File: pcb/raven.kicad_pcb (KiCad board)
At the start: 4 copper layers, 63.2 x 54.2 mm, 144 parts, among them J1 Conn_02x20_Odd_Even, J11 Screw_Terminal_01x10, J14 Conn_01x04_Pin, J15 Conn_01x04_Pin, J16 Conn_01x04_Pin, J17 Conn_01x04_Pin, J18 Conn_01x04_Pin, J2 Conn_01x04_MountingPin, J21 Conn_01x03_Pin, J22 Conn_01x03_Pin, J23 Conn_01x03_Pin, J24 Conn_01x03_Pin, J25 Conn_01x03_Pin, J3 Conn_01x02_Pin, J4 Conn_01x02_Pin, J5 Conn_01x04_MountingPin, J6 Conn_01x02_Pin, J7 Conn_01x02_Pin, J8 Conn_01x02_Pin, J9 Conn_01x02_Pin, U1 DRV8874PWPR, U2 ICM-42688-P, U3 QMC5883L, U30 DRV8874PWPR, U4 DRV8874PWPR, U5 DRV8874PWPR, U6 DRV8874PWPR, U7 STM32G431CBUx, U8 74HC595, Y1 16MHz

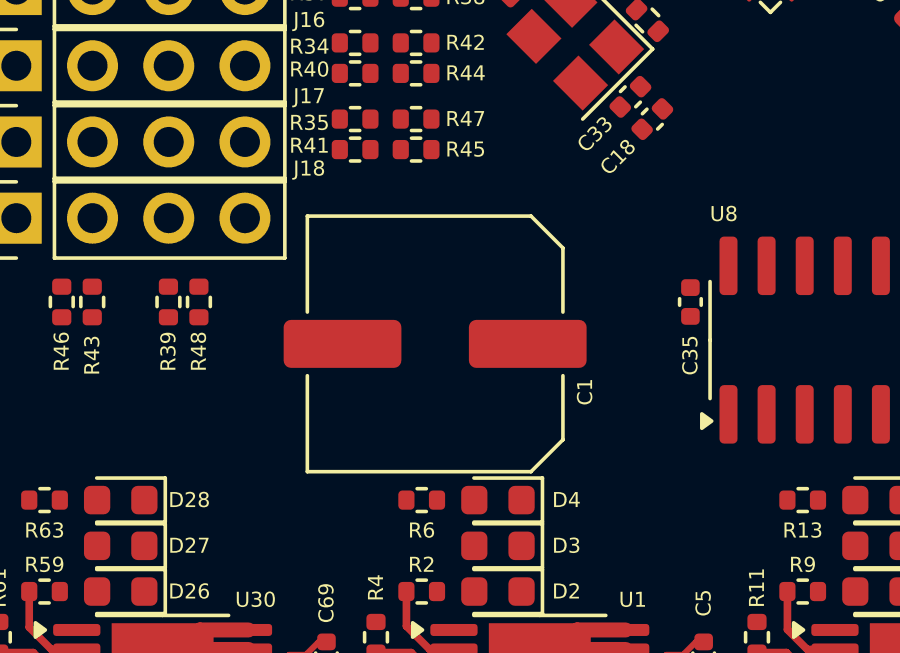
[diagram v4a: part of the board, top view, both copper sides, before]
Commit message: Start on regulator
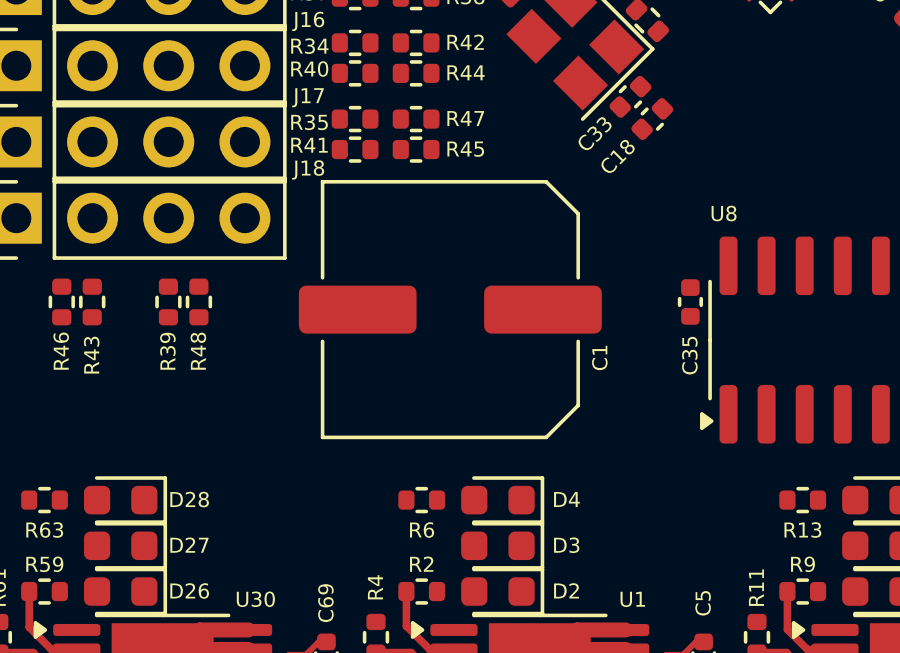
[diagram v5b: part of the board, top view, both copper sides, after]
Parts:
- moved C1 1.25 mm to (113.2, 75.4)

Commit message: Save progress
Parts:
- added C23: 100n, Capacitor_SMD:C_0603_1608Metric, F.Cu at (144.0, 80.4)
- added C39: 100n, Capacitor_SMD:C_0402_1005Metric, F.Cu at (143.2, 71.6)
- added C40: 47u, Capacitor_SMD:C_1206_3216Metric, F.Cu at (142.6, 69.8)
- added C41: 47u, Capacitor_SMD:C_1206_3216Metric, F.Cu at (142.6, 67.4)
- added C42: 47u, Capacitor_SMD:C_1206_3216Metric, F.Cu at (142.6, 65.0)
- added C43: 47u, Capacitor_SMD:C_1206_3216Metric, F.Cu at (142.6, 62.6)
- added C44: 220n, Capacitor_SMD:C_0603_1608Metric, F.Cu at (148.3, 83.4)
- added C45: 2u2, Capacitor_SMD:C_0805_2012Metric, F.Cu at (144.0, 74.0)
- added C46: 1u, Capacitor_SMD:C_0402_1005Metric, F.Cu at (144.4, 78.4)
- added C47: 1u, Capacitor_SMD:C_0402_1005Metric, F.Cu at (143.4, 78.4)
- added C48: 1u, Capacitor_SMD:C_0402_1005Metric, F.Cu at (150.4, 77.0)
- added C49: 1u, Capacitor_SMD:C_0402_1005Metric, F.Cu at (151.4, 77.0)
- added C50: 22u, Capacitor_SMD:C_0805_2012Metric, F.Cu at (153.0, 76.8)
- added C51: 22u, Capacitor_SMD:C_0805_2012Metric, F.Cu at (155.0, 76.8)
- added C52: 22u, Capacitor_SMD:C_0805_2012Metric, F.Cu at (157.0, 76.8)
- added C53: 22u, Capacitor_SMD:C_0805_2012Metric, F.Cu at (159.0, 76.8)
- added C54: 22u, Capacitor_SMD:C_0805_2012Metric, F.Cu at (157.0, 79.5)
- added C57: 22u, Capacitor_SMD:C_0805_2012Metric, F.Cu at (119.0, 82.6)
- added C58: 22u, Capacitor_SMD:C_0805_2012Metric, F.Cu at (131.6, 82.6)
- added C59: 22u, Capacitor_SMD:C_0805_2012Metric, F.Cu at (131.6, 84.6)
- added C60: 22u, Capacitor_SMD:C_0805_2012Metric, F.Cu at (144.0, 82.6)
- added C61: 22u, Capacitor_SMD:C_0805_2012Metric, F.Cu at (144.0, 84.6)
- added C62: 22u, Capacitor_SMD:C_0805_2012Metric, F.Cu at (157.0, 82.5)
- added C63: 22u, Capacitor_SMD:C_0805_2012Metric, F.Cu at (157.0, 84.5)
- added C64: 22u, Capacitor_SMD:C_0805_2012Metric, F.Cu at (106.4, 82.6)
- added C65: 22u, Capacitor_SMD:C_0805_2012Metric, F.Cu at (106.4, 84.6)
- added D14: GLED, LED_SMD:LED_0603_1608Metric, F.Cu at (136.6, 70.2)
- added L1: 330nH, Inductor_SMD:L_Changjiang_FXL0630, F.Cu at (138.6, 75.4)
- added R28: R, Resistor_SMD:R_0402_1005Metric, F.Cu at (146.4, 81.7)
- added R49: R, Resistor_SMD:R_0402_1005Metric, F.Cu at (147.4, 81.7)
- added R50: 1k, Resistor_SMD:R_0402_1005Metric, F.Cu at (139.1, 70.4)
- added R51: R, Resistor_SMD:R_0402_1005Metric, F.Cu at (158.3, 81.0)
- added R52: R, Resistor_SMD:R_0402_1005Metric, F.Cu at (156.2, 81.0)
- added R53: R, Resistor_SMD:R_0402_1005Metric, F.Cu at (149.8, 81.7)
- added R54: R, Resistor_SMD:R_0402_1005Metric, F.Cu at (148.8, 81.7)
- added R55: 10k, Resistor_SMD:R_0402_1005Metric, F.Cu at (102.1, 79.7)
- added SW1: SW_Push, Footprints:TS-1088, F.Cu at (99.4, 77.2)
- added SW2: SW_Push, Footprints:TS-1088, F.Cu at (104.8, 77.2)
- added U9: TPS548B28RWWR, Footprints:TPS548B28RWWR, F.Cu at (147.4, 77.4)
- C13: value 100u -> 22u; footprint Capacitor_SMD:C_Elec_8x6.2 -> Capacitor_SMD:C_0805_2012Metric
- moved J9 23.0 mm to (138.0, 67.2), turned to -90 degrees
- moved C13 23.0 mm to (119.0, 84.6), turned to 180 degrees
- moved J4 22.4 mm to (138.0, 57.0), turned to -90 degrees
- moved J8 22.0 mm to (138.0, 64.6), turned to -90 degrees
- moved J6 21.7 mm to (138.0, 59.5), turned to -90 degrees
- moved J7 21.5 mm to (138.0, 62.1), turned to -90 degrees
- moved R24 8.70 mm to (128.2, 70.2), turned to 90 degrees
- moved R25 8.35 mm to (131.2, 70.2)
- moved C28 7.14 mm to (133.6, 72.4), turned to 180 degrees
- moved J22 5.94 mm to (144.6, 54.5)
- moved J21 5.94 mm to (142.0, 54.5)
- moved J23 5.94 mm to (147.1, 54.5)
- moved J24 5.94 mm to (149.7, 54.5)
- moved J25 5.94 mm to (152.2, 54.5)
- moved R39 3.19 mm to (107.0, 75.2)
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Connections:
- net /BOOT renamed /BT0

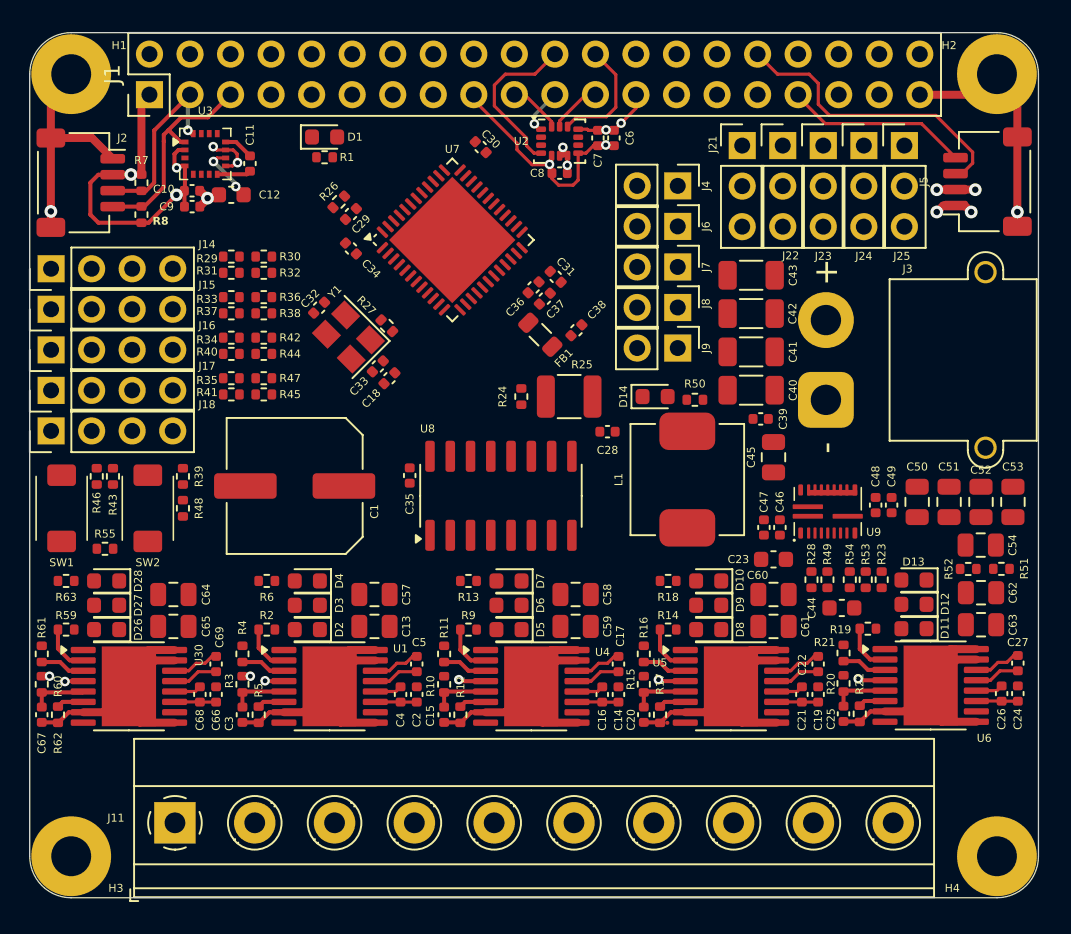
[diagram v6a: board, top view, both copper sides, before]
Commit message: Finish schematic
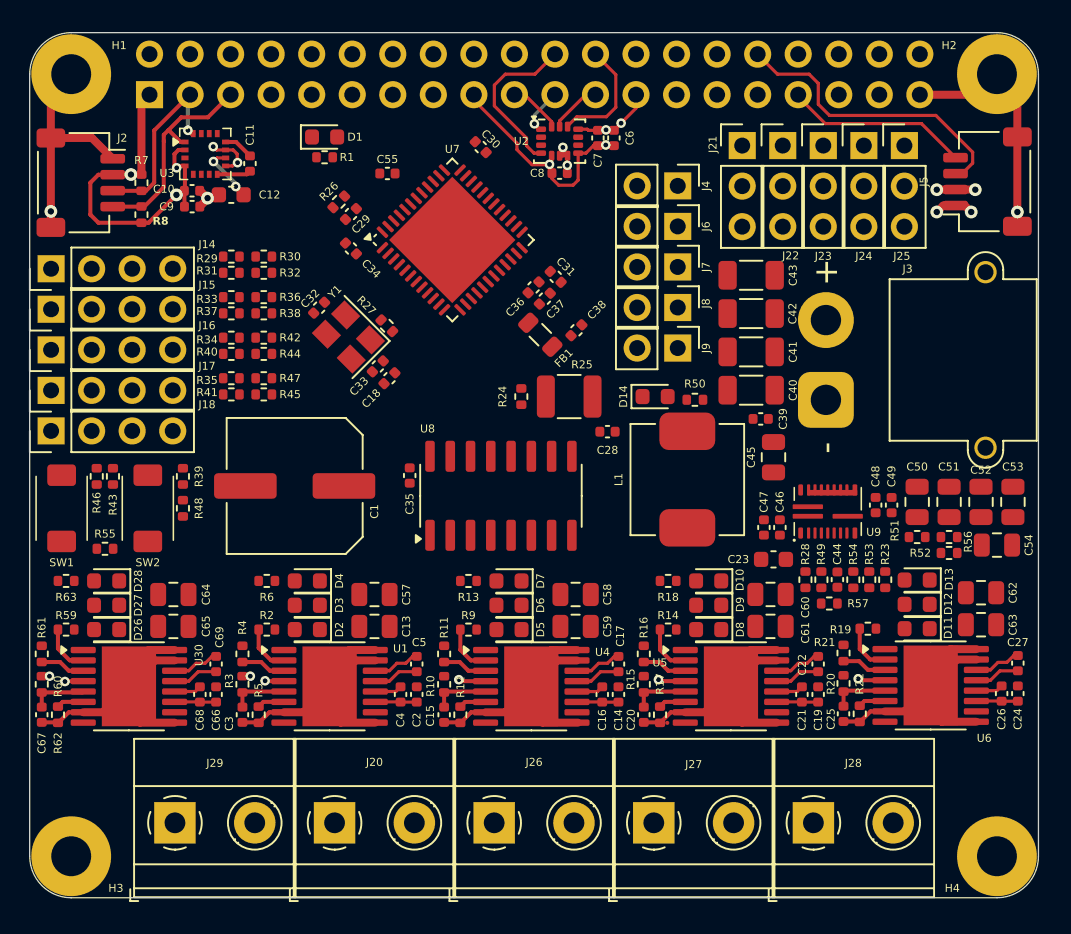
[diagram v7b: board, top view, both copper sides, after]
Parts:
- removed J11: Screw_Terminal_01x10, TerminalBlock_Phoenix:TerminalBlock_Phoenix_MKDS-1,5-10_1x10_P5.00mm_Horizontal
- added C55: 10u, Capacitor_SMD:C_0402_1005Metric, F.Cu at (119.8, 56.2)
- added J20: Screw_Terminal_01x02, TerminalBlock_Phoenix:TerminalBlock_Phoenix_MKDS-1,5-2_1x02_P5.00mm_Horizontal, F.Cu at (116.5, 96.9)
- added J26: Screw_Terminal_01x02, TerminalBlock_Phoenix:TerminalBlock_Phoenix_MKDS-1,5-2_1x02_P5.00mm_Horizontal, F.Cu at (126.5, 96.9)
- added J27: Screw_Terminal_01x02, TerminalBlock_Phoenix:TerminalBlock_Phoenix_MKDS-1,5-2_1x02_P5.00mm_Horizontal, F.Cu at (136.5, 96.9)
- added J28: Screw_Terminal_01x02, TerminalBlock_Phoenix:TerminalBlock_Phoenix_MKDS-1,5-2_1x02_P5.00mm_Horizontal, F.Cu at (146.5, 96.9)
- added J29: Screw_Terminal_01x02, TerminalBlock_Phoenix:TerminalBlock_Phoenix_MKDS-1,5-2_1x02_P5.00mm_Horizontal, F.Cu at (106.5, 96.9)
- added R56: 10k, Resistor_SMD:R_0402_1005Metric, F.Cu at (155.0, 79.0)
- added R57: 47k, Resistor_SMD:R_0402_1005Metric, F.Cu at (147.5, 83.2)
- C44: footprint Capacitor_SMD:C_0603_1608Metric -> Capacitor_SMD:C_0402_1005Metric
- J1: footprint Connector_PinHeader_2.54mm:PinHeader_2x20_P2.54mm_Vertical -> Connector_PinSocket_2.54mm:PinSocket_2x20_P2.54mm_Vertical; moved to B.Cu
- R28, R51, R52, R54: value R -> 10k
- R49: value R -> 200k
- R53: value R -> 75k
- moved R51 5.64 mm to (153.0, 79.0)
- moved C44 1.80 mm to (148.0, 81.7), turned to -90 degrees
- moved R52 1.56 mm to (155.0, 80.0), turned to 0 degrees
- moved C54 1.02 mm to (158.0, 79.5)
- moved R28 0.38 mm to (146.0, 81.7)
- moved R49 0.38 mm to (147.0, 81.7), turned to 90 degrees
- moved R23 0.22 mm to (151.0, 81.7)
- moved R53 0.22 mm to (150.0, 81.7)
- moved R54 0.22 mm to (149.0, 81.7)
- moved D11 0.20 mm to (153.0, 84.7)
- moved D12 0.20 mm to (153.0, 83.2)
- moved D13 0.20 mm to (153.0, 81.7)
- moved C60 0.19 mm to (143.8, 82.6)
- moved C61 0.19 mm to (143.8, 84.6)
- turned J1 to -90 degrees
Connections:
- C44 pad 2: /VSNS -> GND
- R49 pad 1: /MODE -> Net-(R49-Pad1)
- R49 pad 2: GND -> /MD
- R51 pad 1: VDD -> /END
- R54 pad 2: /VSNS -> GND
- U1 pad 10: /MotorHub/OB2 -> /MotorHub/LargeMotor2/OUTB
- U1 pad 8: /MotorHub/OA2 -> /MotorHub/LargeMotor2/OUTA
- U30 pad 10: /MotorHub/OB1 -> /MotorHub/LargeMotor1/OUTB
- U30 pad 8: /MotorHub/OA1 -> /MotorHub/LargeMotor1/OUTA
- U4 pad 10: /MotorHub/OB3 -> /MotorHub/LargeMotor3/OUTB
- U4 pad 8: /MotorHub/OA3 -> /MotorHub/LargeMotor3/OUTA
- U5 pad 10: /MotorHub/OB4 -> /MotorHub/LargeMotor4/OUTB
- U5 pad 8: /MotorHub/OA4 -> /MotorHub/LargeMotor4/OUTA
- U6 pad 10: /MotorHub/OB5 -> /MotorHub/LargeMotor5/OUTB
- U6 pad 8: /MotorHub/OA5 -> /MotorHub/LargeMotor5/OUTA
- U9 pad 4: /MODE -> /MD
- U9 pad 6: /VSNS -> GND

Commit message: Start wiring
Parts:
- added J10: Conn_ARM_SWD_TagConnect_TC2030-NL, Connector:Tag-Connect_TC2030-IDC-NL_2x03_P1.27mm_Vertical, F.Cu at (121.7, 44.0)
- moved R21 3.68 mm to (150.5, 83.2), turned to 180 degrees
- moved R4 3.40 mm to (112.3, 83.3), turned to 180 degrees
- moved R16 3.39 mm to (137.4, 83.3), turned to 180 degrees
- moved R61 3.39 mm to (99.7, 83.3), turned to 180 degrees
- moved R11 3.39 mm to (124.9, 83.3), turned to 180 degrees
- moved R23 1.89 mm to (152.4, 80.4), turned to 180 degrees
- moved C2 1.46 mm to (122.3, 90.1), turned to -90 degrees
- moved C66 1.44 mm to (109.7, 90.2), turned to -90 degrees
- moved C24 1.42 mm to (159.9, 90.1), turned to -90 degrees
- moved C14 1.40 mm to (134.9, 90.1), turned to -90 degrees
- moved C19 1.35 mm to (147.4, 90.1), turned to -90 degrees
- moved C22 1.15 mm to (145.7, 86.5), turned to 90 degrees
- moved C27 1.14 mm to (158.3, 86.4), turned to 90 degrees
- moved C17 1.13 mm to (133.3, 86.5), turned to 90 degrees
- moved C5 1.12 mm to (120.6, 86.5), turned to 90 degrees
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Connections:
- J3 pad : (no net) -> GND
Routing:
- net GND: track 141.0 -> 101.7 mm, vias 11 -> 25
- net /MotorHub/Encoder4/BIN: track 0.00 -> 12.7 mm
- net /MotorHub/Encoder2/BIN: track 0.00 -> 11.2 mm
- net /MotorHub/Encoder2/AIN: track 0.00 -> 10.2 mm
- net /MotorHub/Encoder1/BIN: track 0.00 -> 9.86 mm
- net /MotorHub/LargeMotor1/FLT: track 1.15 -> 11.0 mm, vias 1 -> 2
- net /MotorHub/LargeMotor5/FLT: track 1.72 -> 11.4 mm, vias 1 -> 2
- net /MotorHub/LargeMotor3/FLT: track 1.72 -> 11.1 mm, vias 1 -> 2
- net /MotorHub/LargeMotor4/FLT: track 1.72 -> 11.0 mm, vias 1 -> 2
- net /MotorHub/Encoder3/BIN: track 0.00 -> 9.18 mm
- net /MotorHub/Encoder1/AIN: track 0.00 -> 7.61 mm
- net /EN: track 0.00 -> 7.32 mm
- net /MotorHub/Encoder4/AIN: track 0.00 -> 7.07 mm
- net /MotorHub/Encoder3/AIN: track 0.00 -> 6.44 mm
- net VDD: track 13.0 -> 6.58 mm
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- added copper zone on F.Cu, net +5V
- added copper zone on F.Cu, net /MotorHub/LargeMotor1/OUTA
- added copper zone on F.Cu, net /MotorHub/LargeMotor1/OUTB
- added copper zone on F.Cu, net /MotorHub/LargeMotor2/OUTA
- added copper zone on F.Cu, net /MotorHub/LargeMotor2/OUTB
- added copper zone on F.Cu, net /MotorHub/LargeMotor3/OUTA
- added copper zone on F.Cu, net /MotorHub/LargeMotor3/OUTB
- added copper zone on F.Cu, net /MotorHub/LargeMotor4/OUTA
- added copper zone on F.Cu, net /MotorHub/LargeMotor4/OUTB
- added copper zone on F.Cu, net /MotorHub/LargeMotor5/OUTA
- added copper zone on F.Cu, net /MotorHub/LargeMotor5/OUTB
- added copper zone on F.Cu, net /SW
- added copper zone on F.Cu, net GND
- added copper zone on F.Cu, net VDD
